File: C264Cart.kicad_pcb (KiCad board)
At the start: 2 copper layers, 55.8 x 64.7 mm, 14 parts, among them U1 27C040, U3 264-Exp-Port

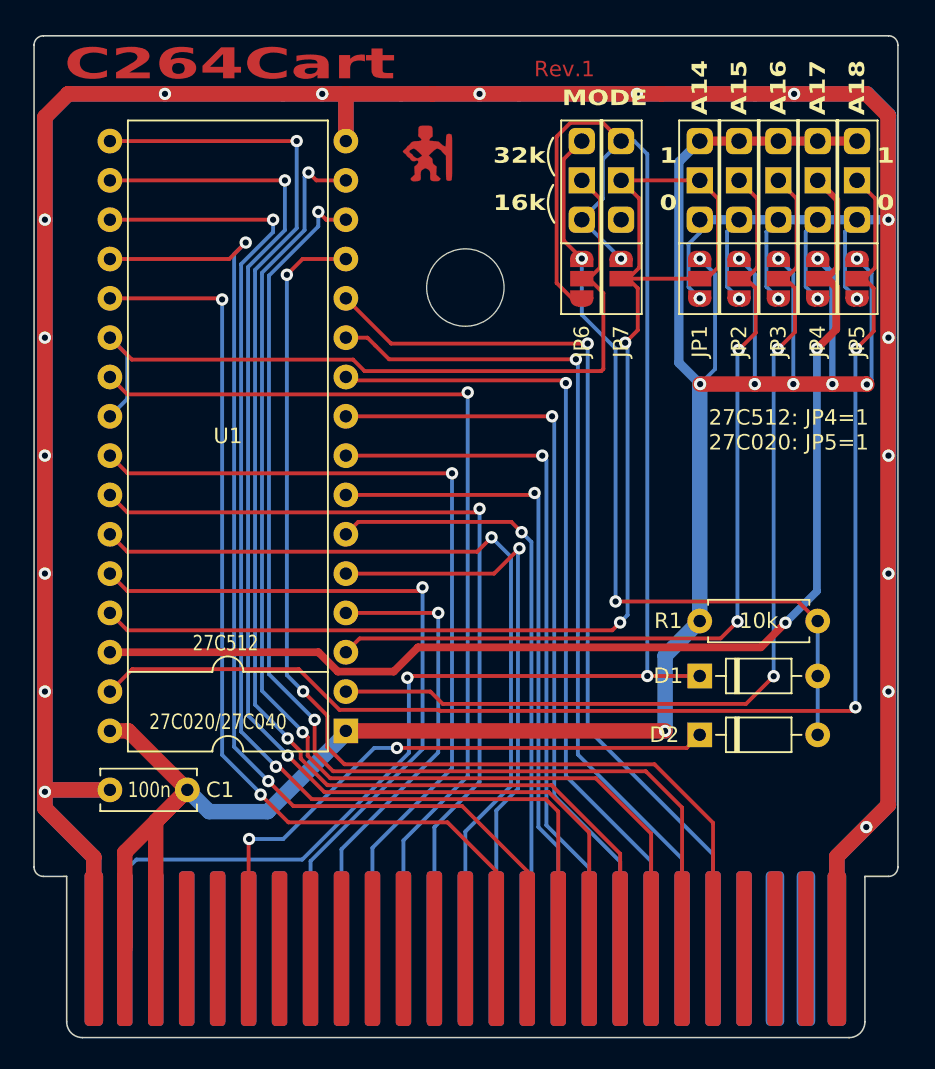
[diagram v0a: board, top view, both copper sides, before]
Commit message: updated to SMD components (except EPROM)
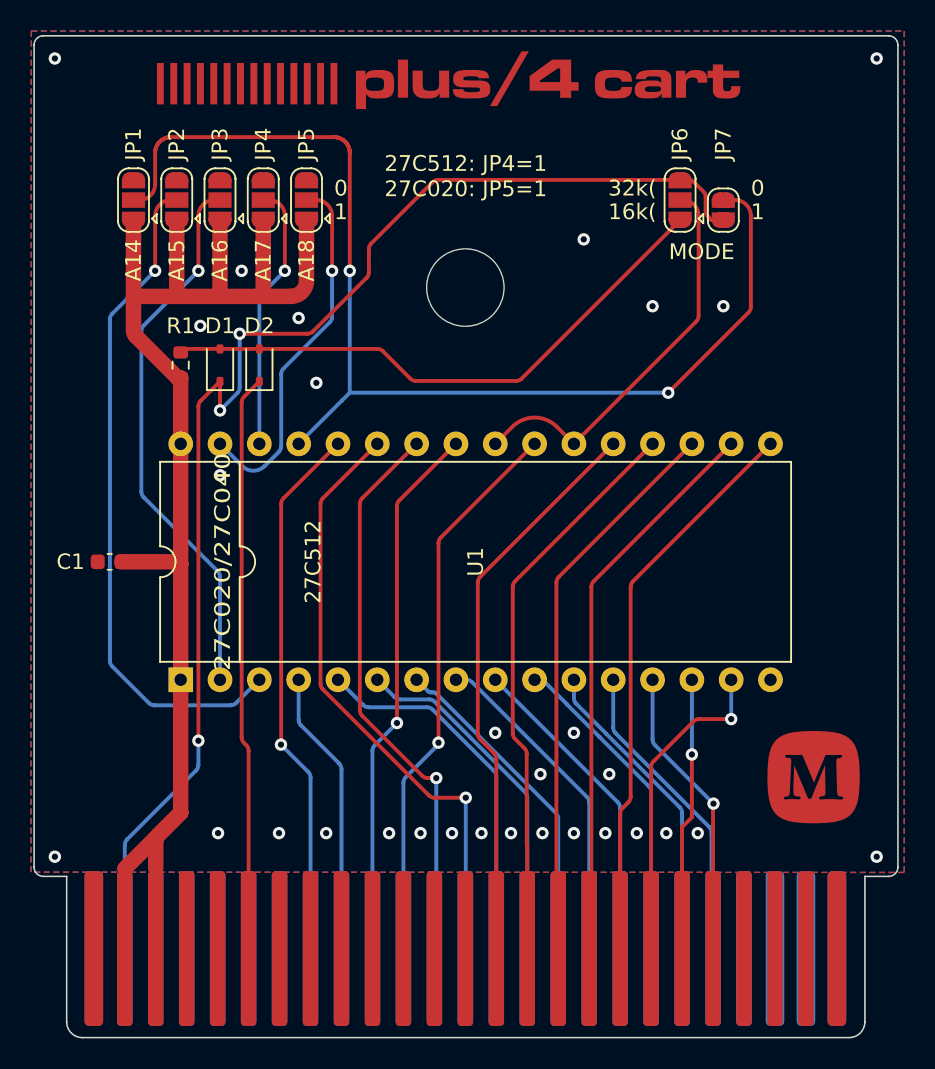
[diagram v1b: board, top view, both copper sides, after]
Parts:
- removed G***: LOGO, Logo:bigby2-cu
- C1: footprint Capacitor_THT:C_Disc_D6.0mm_W2.5mm_P5.00mm -> Capacitor_SMD:C_0603_1608Metric
- D1, D2: footprint Diode_THT:D_DO-35_SOD27_P7.62mm_Horizontal -> Diode_SMD:D_SOD-323
- JP1, JP2, JP3, JP4, JP5, JP6: footprint C264Cart:Jumper3_Solder -> Jumper:SolderJumper-3_P1.3mm_Open_RoundedPad1.0x1.5mm
- JP7: footprint C264Cart:Jumper3_Solder -> Jumper:SolderJumper-2_P1.3mm_Open_RoundedPad1.0x1.5mm
- R1: footprint Resistor_THT:R_Axial_DIN0207_L6.3mm_D2.5mm_P7.62mm_Horizontal -> Resistor_SMD:R_0603_1608Metric
- moved R1 37.4 mm to (111.5, 92.4), turned to 90 degrees
- moved D2 37.1 mm to (116.6, 92.4), turned to 90 degrees
- moved D1 36.9 mm to (114.1, 92.4), turned to 90 degrees
- moved JP1 36.8 mm to (108.5, 81.7), turned to 90 degrees
- moved JP2 36.5 mm to (111.3, 81.7), turned to 90 degrees
- moved JP3 36.3 mm to (114.1, 81.7), turned to 90 degrees
- moved JP4 36.0 mm to (116.9, 81.7), turned to 90 degrees
- moved JP5 35.8 mm to (119.7, 81.7), turned to 90 degrees
- moved C1 15.6 mm to (106.9, 105.1)
- moved U1 11.2 mm to (111.5, 112.7), turned to 90 degrees
- moved JP7 7.97 mm to (146.6, 82.4), turned to 90 degrees
- moved JP6 7.41 mm to (143.8, 81.7), turned to 90 degrees
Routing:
- net GND: track 387.3 -> 0.00 mm, vias 22 -> 30
- net +5V: track 167.6 -> 83.4 mm, vias 11 -> 0
- net /A18: track 86.0 -> 23.7 mm, vias 2 -> 1
- net /D1: track 73.8 -> 12.8 mm, vias 2 -> 1
- net /A17: track 77.6 -> 17.3 mm, vias 2 -> 1
- net /D2: track 74.5 -> 16.0 mm, vias 2 -> 1
- net /D0: track 70.9 -> 14.2 mm, vias 2 -> 1
- net /D3: track 83.6 -> 31.8 mm, vias 2 -> 0
- net /D4: track 79.5 -> 31.7 mm, vias 2 -> 0
- net /D5: track 76.0 -> 31.4 mm, vias 2 -> 0
- net /A0: track 59.3 -> 15.3 mm, vias 1 -> 0
- net /A1: track 56.3 -> 15.4 mm, vias 1 -> 0
- net /D6: track 69.4 -> 31.9 mm, vias 2 -> 0
- net /A2: track 53.2 -> 15.9 mm, vias 1 -> 0
- net /A3: track 49.5 -> 15.9 mm, vias 1 -> 0
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- added copper zone on B.Cu, net GND
- added copper zone on F.Cu, net GND
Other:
- board text added: "16k("
- board text added: "32k("
- board text added: "A14"
- board text added: "A15"
- board text added: "A16"
- board text added: "A17"
- board text added: "A18"
- board text added: "WAYWAYWAY"
- board text added: "github.com/fastjack/plus4cart"
- board text removed: "16k"
- board text removed: "32k"
- board text removed: "C264Cart"
- board text removed: "JLCJLCJLCJLC"
- board text removed: "Rev.1"
- board text removed: "github.com/hackup/C264Cart"
